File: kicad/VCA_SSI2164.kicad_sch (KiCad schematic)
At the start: 9 parts, among them U10 TL072, U4 SSI2164, U7 SSI2164

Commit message: added gain calc pdfs
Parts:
- added NT10, NT11, NT12, NT13, NT14, NT15, NT16, NT9: NetTie_2, symbol Device:NetTie_2
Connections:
- net -2V5 is gone; now on net -5V: U10.4 (V-)
- new net: C31.1, NT13.2, NT14.2, NT15.2, NT16.2, R15.1, U10.6 (-)
- new net: NT16.1, U7.13 (I_OUT4)
- new net: C30.1, NT10.2, NT11.2, NT12.2, NT9.2, R10.1, U10.2 (-)
- new net: NT12.1, U4.13 (I_OUT4)
- new net: NT11.1, U4.12 (I_OUT3)
- new net: NT9.1, U4.4 (I_OUT1)
- new net: NT10.1, U4.5 (I_OUT2)
- new net: NT15.1, U7.12 (I_OUT3)
- new net: NT13.1, U7.4 (I_OUT1)
- new net: NT14.1, U7.5 (I_OUT2)
- no-connect marks 0 -> 2
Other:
- note added: "Class AB Mode"

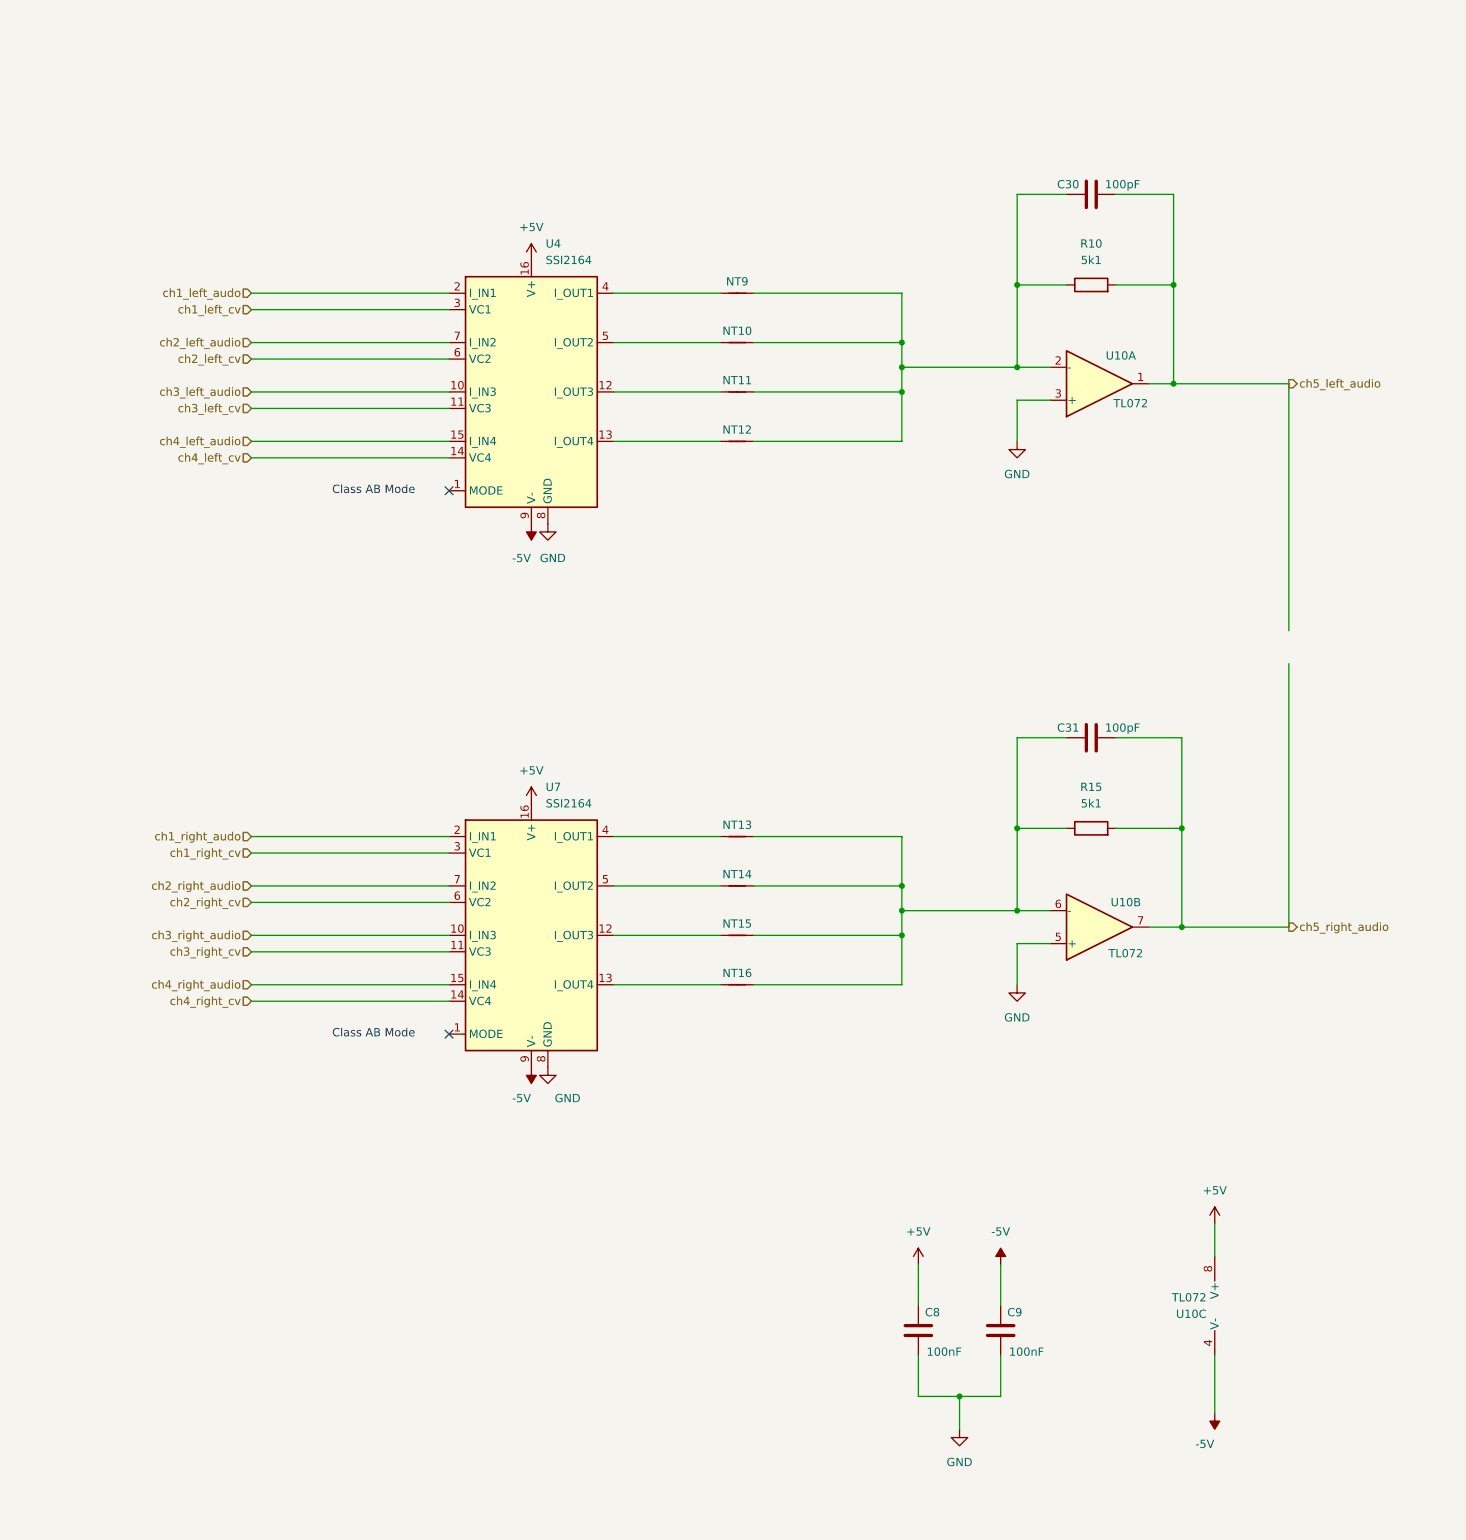
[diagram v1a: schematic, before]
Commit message: Added RC networks to VCAs
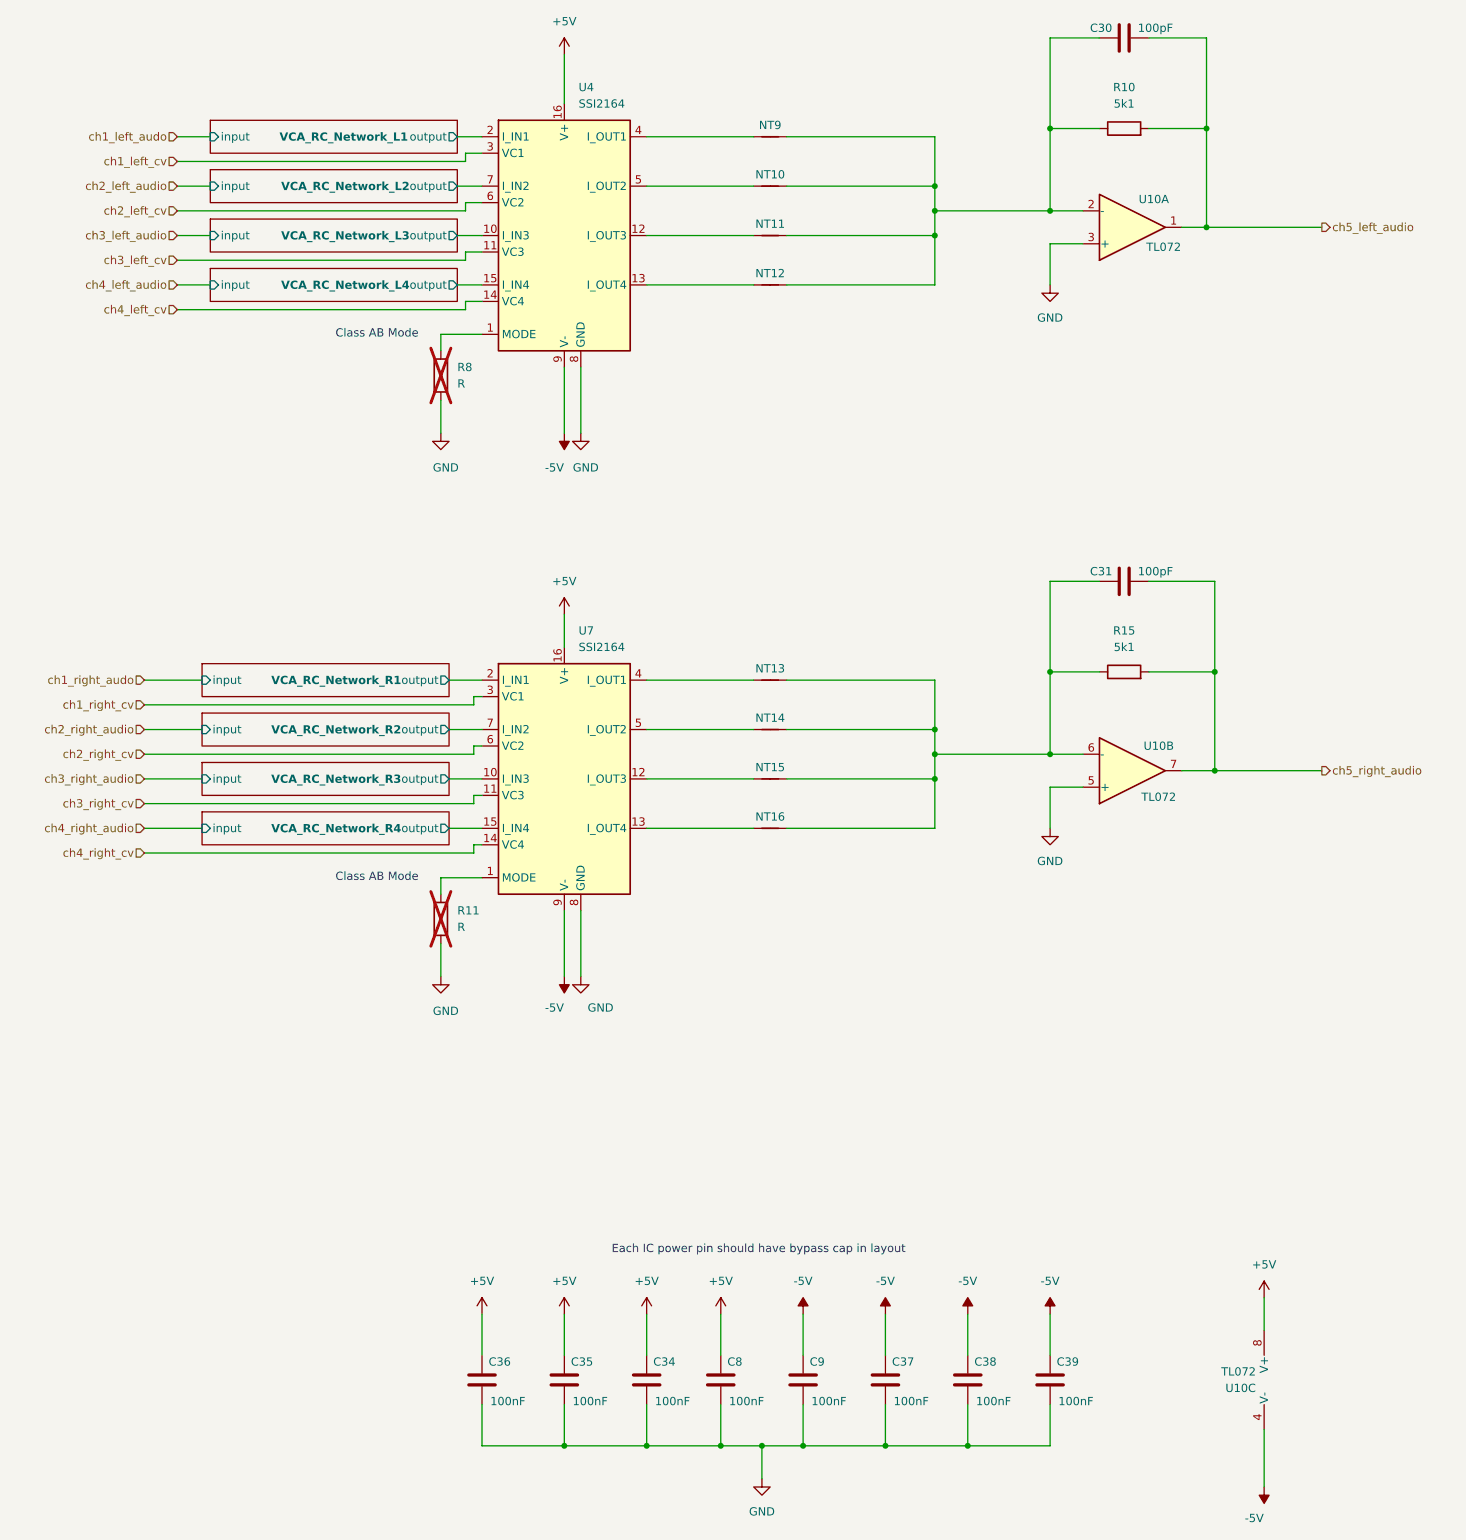
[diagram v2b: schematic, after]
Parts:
- added C34, C35, C36, C37, C38, C39: 100nF, Capacitor_SMD:C_0402_1005Metric_Pad0.74x0.62mm_HandSolder, symbol Device:C
- added R11, R8: R, symbol Device:R
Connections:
- net +5V: now also C34.1, C35.1, C36.1
- net -5V: now also C37.1, C38.1, C39.1
- net GND: now also C34.2, C35.2, C36.2, C37.2, C38.2, C39.2, R11.2, R8.2
- net ch1_left_audo: no longer U4.2 (I_IN1)
- net ch1_right_audo: no longer U7.2 (I_IN1)
- net ch2_left_audio: no longer U4.7 (I_IN2)
- net ch2_right_audio: no longer U7.7 (I_IN2)
- net ch3_left_audio: no longer U4.10 (I_IN3)
- net ch3_right_audio: no longer U7.10 (I_IN3)
- net ch4_left_audio: no longer U4.15 (I_IN4)
- net ch4_right_audio: no longer U7.15 (I_IN4)
- net at U4.1 (MODE): now also R8.1
- net at U7.1 (MODE): now also R11.1
- new net VCA_RC_Network_L1/output: U4.2 (I_IN1)
- new net VCA_RC_Network_L2/output: U4.7 (I_IN2)
- new net VCA_RC_Network_L3/output: U4.10 (I_IN3)
- new net VCA_RC_Network_L4/output: U4.15 (I_IN4)
- new net VCA_RC_Network_R1/output: U7.2 (I_IN1)
- new net VCA_RC_Network_R2/output: U7.7 (I_IN2)
- new net VCA_RC_Network_R3/output: U7.10 (I_IN3)
- new net VCA_RC_Network_R4/output: U7.15 (I_IN4)
- no-connect marks 2 -> 0
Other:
- added sheet VCA_RC_Network_L1 (vca_rc_network.kicad_sch)
- added sheet VCA_RC_Network_L2 (vca_rc_network.kicad_sch)
- added sheet VCA_RC_Network_L3 (vca_rc_network.kicad_sch)
- added sheet VCA_RC_Network_L4 (vca_rc_network.kicad_sch)
- added sheet VCA_RC_Network_R1 (vca_rc_network.kicad_sch)
- added sheet VCA_RC_Network_R2 (vca_rc_network.kicad_sch)
- added sheet VCA_RC_Network_R3 (vca_rc_network.kicad_sch)
- added sheet VCA_RC_Network_R4 (vca_rc_network.kicad_sch)
- note added: "Each IC power pin should have bypass cap in layout"
- moved on the sheet: C30, C31, C8, C9, NT10, NT11, NT12, NT13, NT14, NT15, NT16, NT9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
